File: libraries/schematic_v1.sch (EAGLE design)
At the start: 46 parts, among them Q1 BSS138, Q2 BSS138, Q3 BSS138, Q4 BSS138

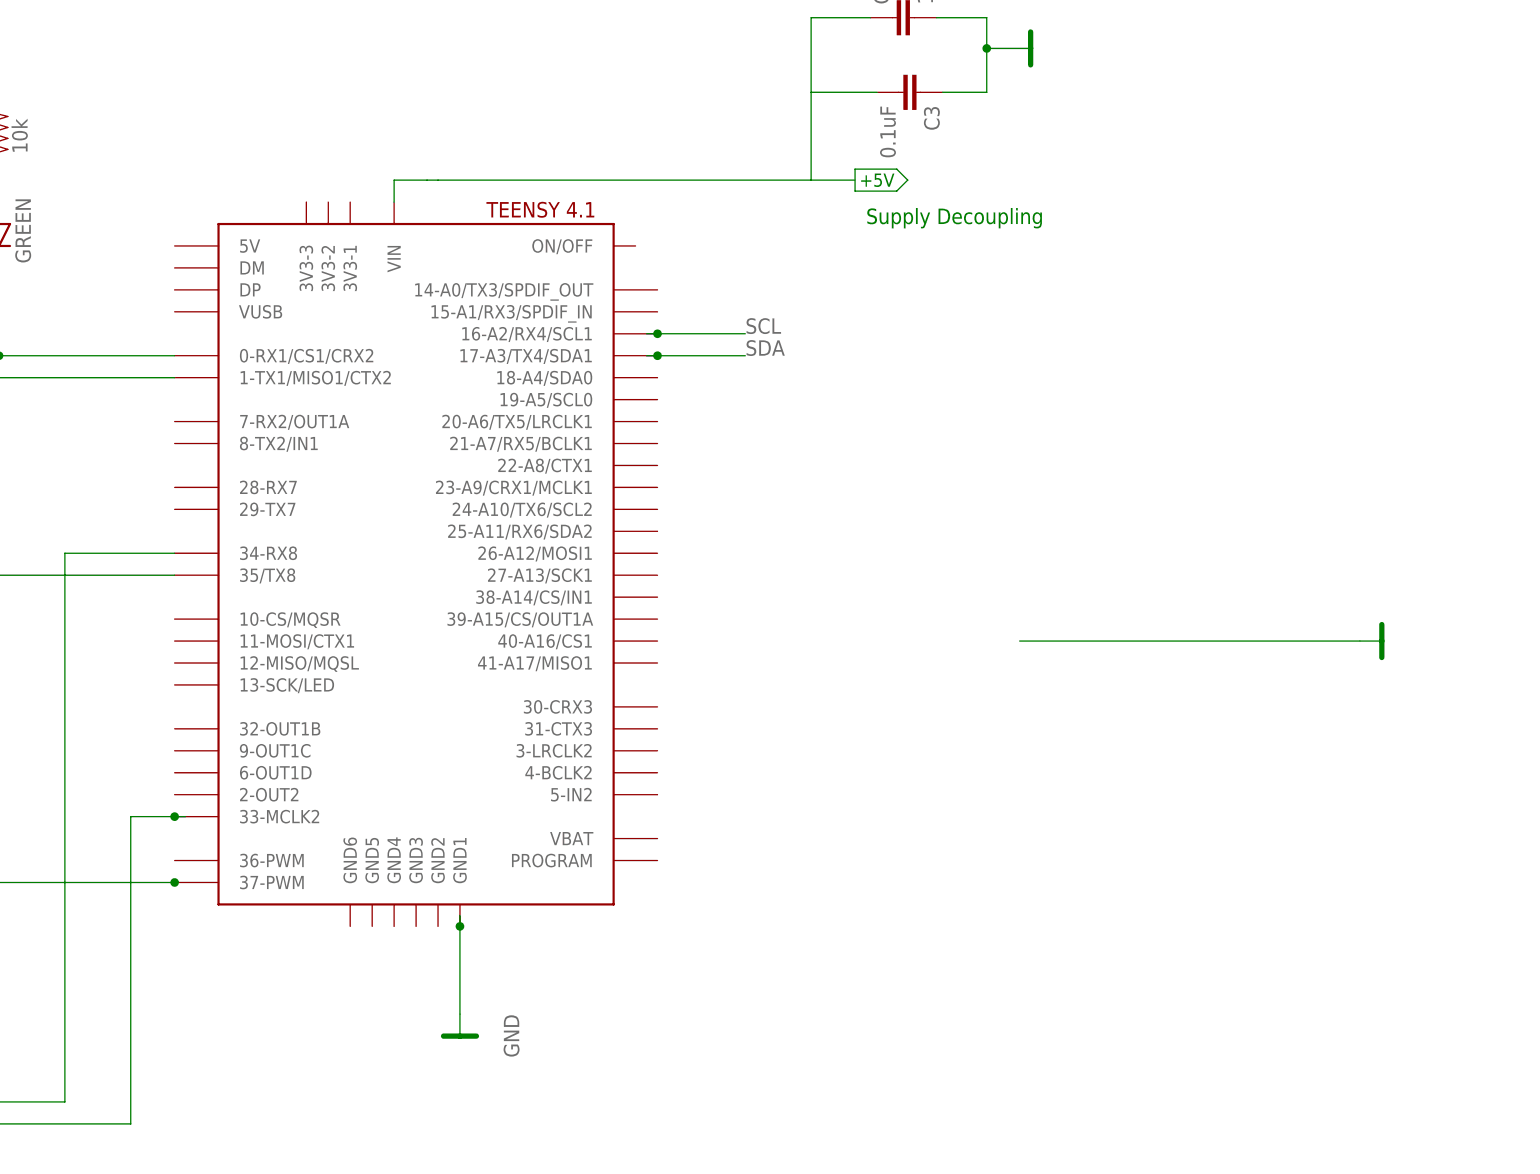
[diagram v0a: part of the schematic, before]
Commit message: new teensy 4.1 footprint
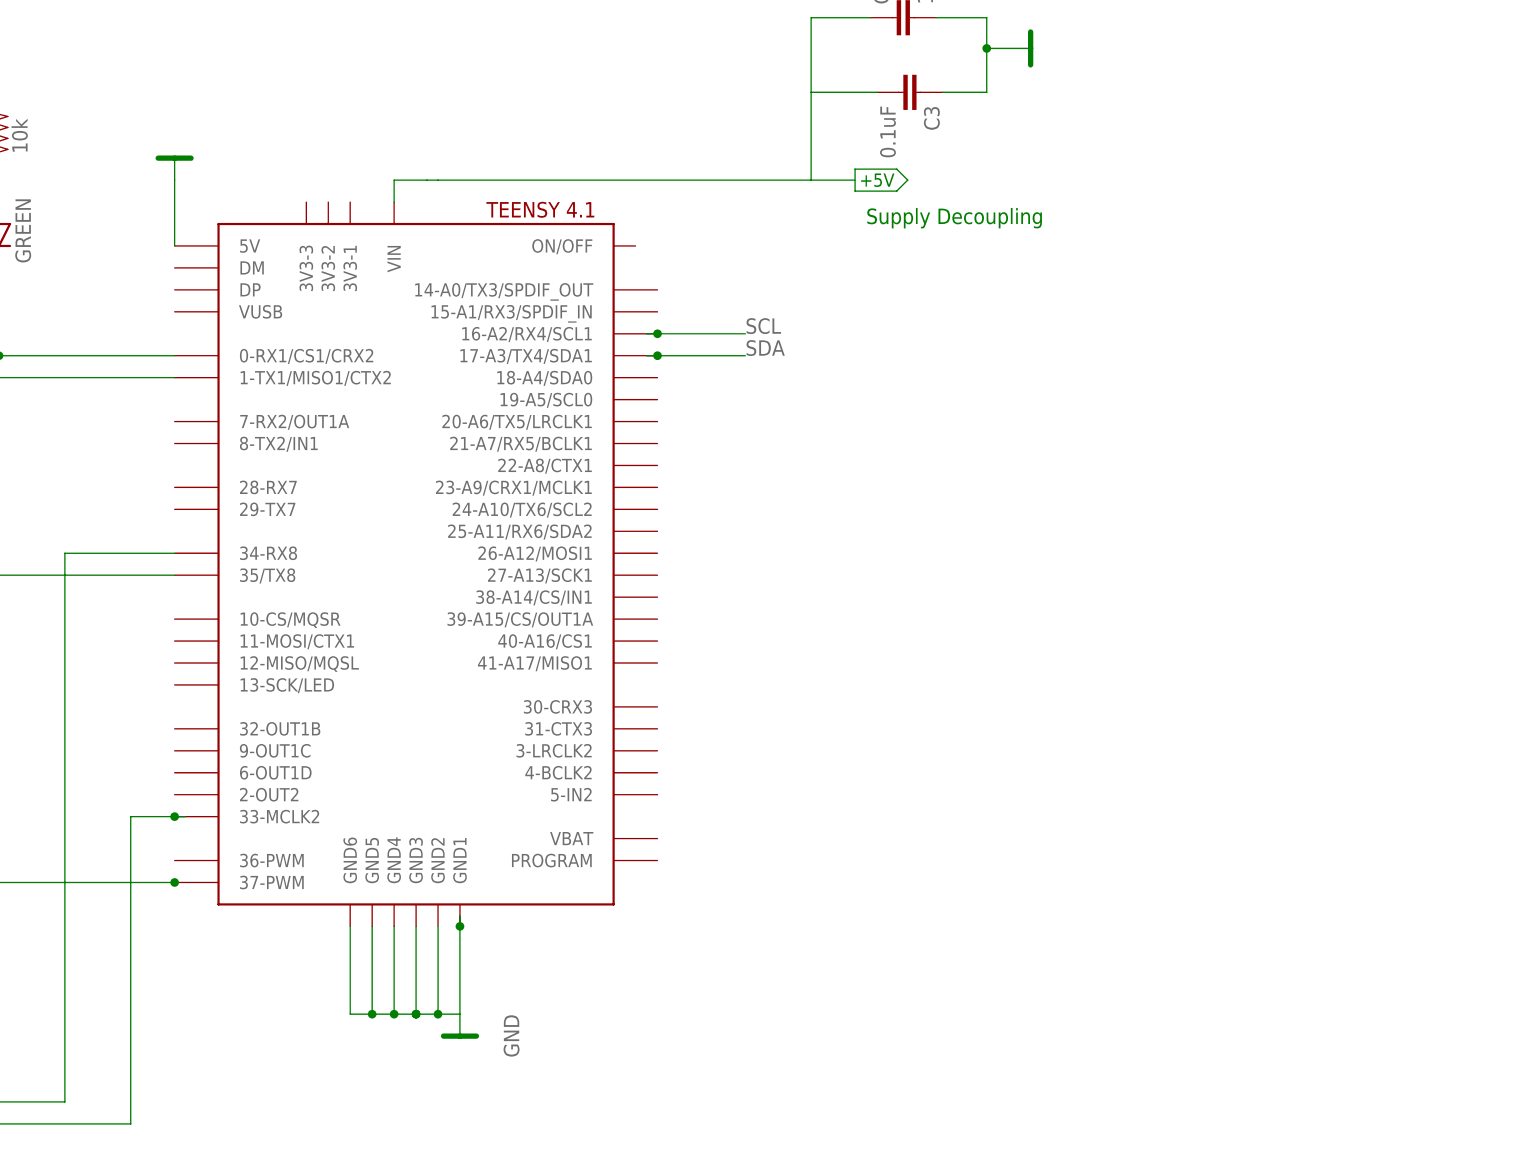
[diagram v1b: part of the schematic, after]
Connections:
- net GND: now also U$4.5V, U$4.GND2, U$4.GND3, U$4.GND4, U$4.GND5, U$4.GND6
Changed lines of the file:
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@@
 </instance>
 <instance part="GND3" gate="VR1" x="99.06" y="99.06" smashed="yes" rot="R90"/>
-<instance part="GND5" gate="VR1" x="139.7" y="30.48" smashed="yes" rot="R90"/>
+<instance part="GND5" gate="VR1" x="0" y="86.36" smashed="yes" rot="R180"/>
 <instance part="U$2" gate="G$1" x="63.5" y="167.64" smashed="yes" grouprefs="POWER">
 <attribute name="NAME" x="58.674" y="173.99" size="1.778" layer="95"/>
@@
 <wire x1="33.02" y1="-2.54" x2="33.02" y2="-1.27" width="0.1524" layer="91"/>
 <junction x="33.02" y="-2.54"/>
+<pinref part="U$4" gate="G$1" pin="GND2"/>
+<wire x1="33.02" y1="-12.7" x2="30.48" y2="-12.7" width="0.1524" layer="91"/>
+<wire x1="30.48" y1="-12.7" x2="30.48" y2="-2.54" width="0.1524" layer="91"/>
+<junction x="27.94" y="-12.7"/>
+<pinref part="U$4" gate="G$1" pin="GND3"/>
+<wire x1="30.48" y1="-12.7" x2="27.94" y2="-12.7" width="0.1524" layer="91"/>
+<wire x1="27.94" y1="-12.7" x2="27.94" y2="-2.54" width="0.1524" layer="91"/>
+<junction x="30.48" y="-12.7"/>
+<pinref part="U$4" gate="G$1" pin="GND4"/>
+<wire x1="27.94" y1="-12.7" x2="25.4" y2="-12.7" width="0.1524" layer="91"/>
+<wire x1="25.4" y1="-12.7" x2="25.4" y2="-2.54" width="0.1524" layer="91"/>
+<junction x="27.94" y="-12.7"/>
+<pinref part="U$4" gate="G$1" pin="GND5"/>
+<wire x1="25.4" y1="-12.7" x2="22.86" y2="-12.7" width="0.1524" layer="91"/>
+<wire x1="22.86" y1="-12.7" x2="22.86" y2="-2.54" width="0.1524" layer="91"/>
+<junction x="25.4" y="-12.7"/>
+<pinref part="U$4" gate="G$1" pin="GND6"/>
+<wire x1="22.86" y1="-12.7" x2="20.32" y2="-12.7" width="0.1524" layer="91"/>
+<wire x1="20.32" y1="-12.7" x2="20.32" y2="-2.54" width="0.1524" layer="91"/>
+<junction x="22.86" y="-12.7"/>
 </segment>
 <segment>
@@
 <segment>
 <pinref part="GND5" gate="VR1" pin="GND"/>
-<wire x1="97.79" y1="30.48" x2="137.16" y2="30.48" width="0.1524" layer="91"/>
-</segment>
-<segment>
+<pinref part="U$4" gate="G$1" pin="5V"/>
+<wire x1="0" y1="76.2" x2="0" y2="83.82" width="0.1524" layer="91"/>
+</segment>
+<segment>
